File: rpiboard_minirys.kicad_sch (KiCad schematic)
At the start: 42 parts, among them IC1 LM51231QRGRRQ1, J1 Conn_01x01_Pin, J2 Conn_01x01_Pin, J3 Conn_01x01_Pin, J4 Conn_01x01_Pin, J6 MCU_Connector, Q1 ISK057N04LM6ATLA1, Q2 ISK057N04LM6ATLA1

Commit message: Added required connectors for this version
Also did some file name changes
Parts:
- removed J1, J2, J3, J4: Conn_01x01_Pin, TestPoint:TestPoint_Pad_2.0x2.0mm, symbol Connector:Conn_01x01_Pin
- removed J6: MCU_Connector, Connector_PinSocket_2.54mm:PinSocket_1x04_P2.54mm_Vertical, symbol Connector:Conn_01x04_Pin
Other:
- sheet 5V_Logic_Power renamed Supply_5V
- sheet Capacitor_Banks renamed Supply_24V_Capacitor_Banks
- sheet RPi_Connectors renamed Connectors
- sheet Connectors: file rpi_connectors.kicad_sch -> connectors.kicad_sch
- sheet Connectors ports: added +5V; removed none
- sheet Supply_24V_Capacitor_Banks: file capacitor_banks.kicad_sch -> s24v_capacitor_banks.kicad_sch
- sheet Supply_5V: file 5v_logic_power.kicad_sch -> supply_5v.kicad_sch
- sheet Supply_5V ports: added +5V; removed none
- note removed: "MCU Connector"
- title: Power Supply Module with 24V+5V output -> 24V Supply
- moved on the sheet: C5, C6, C8, R10, R11, R12, R3, R4, R5, R8, R9, TP4

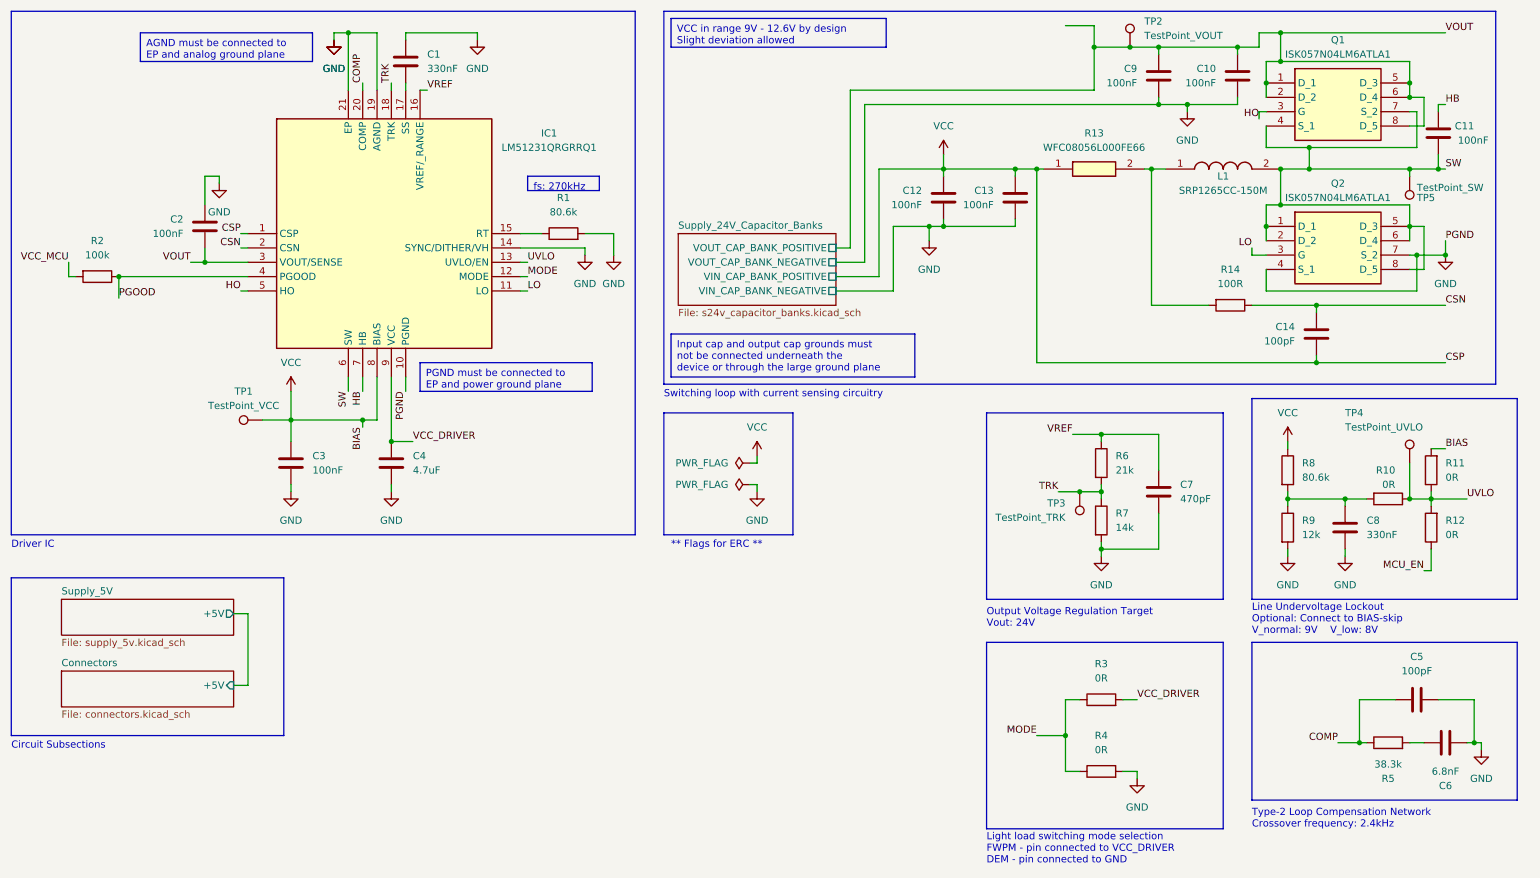
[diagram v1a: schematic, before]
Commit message: Finished motor drivers schematic
Still need to connect all the connectors and sort out old unused connections
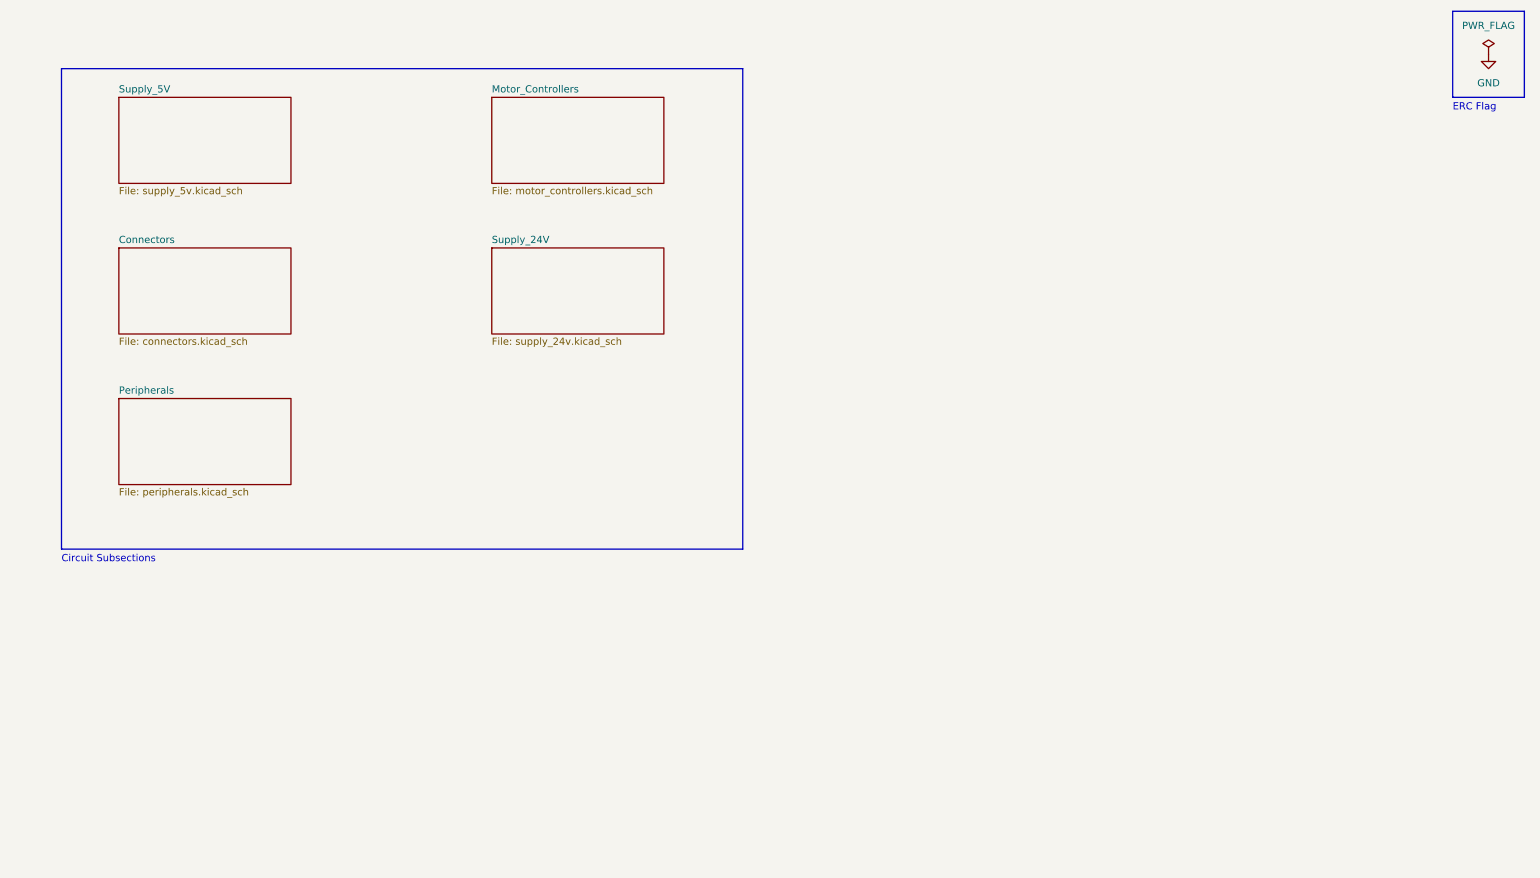
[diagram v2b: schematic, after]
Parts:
- removed C1, C8: 330nF, Capacitor_SMD:C_0603_1608Metric, symbol Device:C
- removed C10, C11, C12, C13, C2, C3, C9: 100nF, Capacitor_SMD:C_0603_1608Metric, symbol Device:C
- removed C14, C5: 100pF, Capacitor_SMD:C_0603_1608Metric, symbol Device:C
- removed C4: 4.7uF, Capacitor_SMD:C_0805_2012Metric, symbol Device:C
- removed C6: 6.8nF, Capacitor_SMD:C_0603_1608Metric, symbol Device:C
- removed C7: 470pF, Capacitor_SMD:C_0603_1608Metric, symbol Device:C
- removed IC1: LM51231QRGRRQ1, parts:QFN50P350X350X100-21N-D, symbol parts:LM51231QRGRRQ1
- removed L1: SRP1265CC-150M, parts:INDPM135125X650N, symbol parts:SRP1265CC-150M
- removed Q1: ISK057N04LM6ATLA1, parts:ISK057N04LM6ATLA1, symbol parts:ISK057N04LM6ATLA1
- removed Q2: ISK057N04LM6ATLA1, parts:ISK057N04LM6ATLA1, symbol SamacSys_Parts:ISK057N04LM6ATLA1
- removed R1, R8: 80.6k, Resistor_SMD:R_0603_1608Metric, symbol Device:R
- removed R10, R11, R12, R3, R4: 0R, Resistor_SMD:R_0603_1608Metric, symbol Device:R
- removed R13: WFC08056L000FE66, parts:RESC2013X85N, symbol parts:WFC08056L000FE66
- removed R14: 100R, Resistor_SMD:R_0603_1608Metric, symbol Device:R
- removed R2: 100k, Resistor_SMD:R_0603_1608Metric, symbol Device:R
- removed R5: 38.3k, Resistor_SMD:R_0603_1608Metric, symbol Device:R
- removed R6: 21k, Resistor_SMD:R_0603_1608Metric, symbol Device:R
- removed R7: 14k, Resistor_SMD:R_0603_1608Metric, symbol Device:R
- removed R9: 12k, Resistor_SMD:R_0603_1608Metric, symbol Device:R
- removed TP1: TestPoint_VCC, TestPoint:TestPoint_Pad_D1.0mm, symbol Connector:TestPoint
- removed TP2: TestPoint_VOUT, TestPoint:TestPoint_Pad_D1.0mm, symbol Connector:TestPoint
- removed TP3: TestPoint_TRK, TestPoint:TestPoint_Pad_D1.0mm, symbol Connector:TestPoint
- removed TP4: TestPoint_UVLO, TestPoint:TestPoint_Pad_D1.0mm, symbol Connector:TestPoint
- removed TP5: TestPoint_SW, TestPoint:TestPoint_Pad_D1.0mm, symbol Connector:TestPoint
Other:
- removed sheet Supply_24V_Capacitor_Banks
- added sheet Motor_Controllers (motor_controllers.kicad_sch)
- added sheet Peripherals (peripherals.kicad_sch)
- added sheet Supply_24V (supply_24v.kicad_sch)
- sheet Connectors ports: added none; removed +5V
- sheet Supply_5V ports: added none; removed +5V
- note added: "ERC Flag"
- note removed: "** Flags for ERC **"
- note removed: "Driver IC"
- note removed: "Light load switching mode selection FWPM - pin connected to VCC_DRIVER DEM - pin connected to GND"
- note removed: "Line Undervoltage Lockout Optional: Connect to BIAS-skip V_normal: 9V V_low: 8V"
- note removed: "Output Voltage Regulation Target Vout: 24V"
- note removed: "Switching loop with current sensing circuitry"
- note removed: "Type-2 Loop Compensation Network Crossover frequency: 2.4kHz"
- title: 24V Supply -> RPi Hat for MiniRys

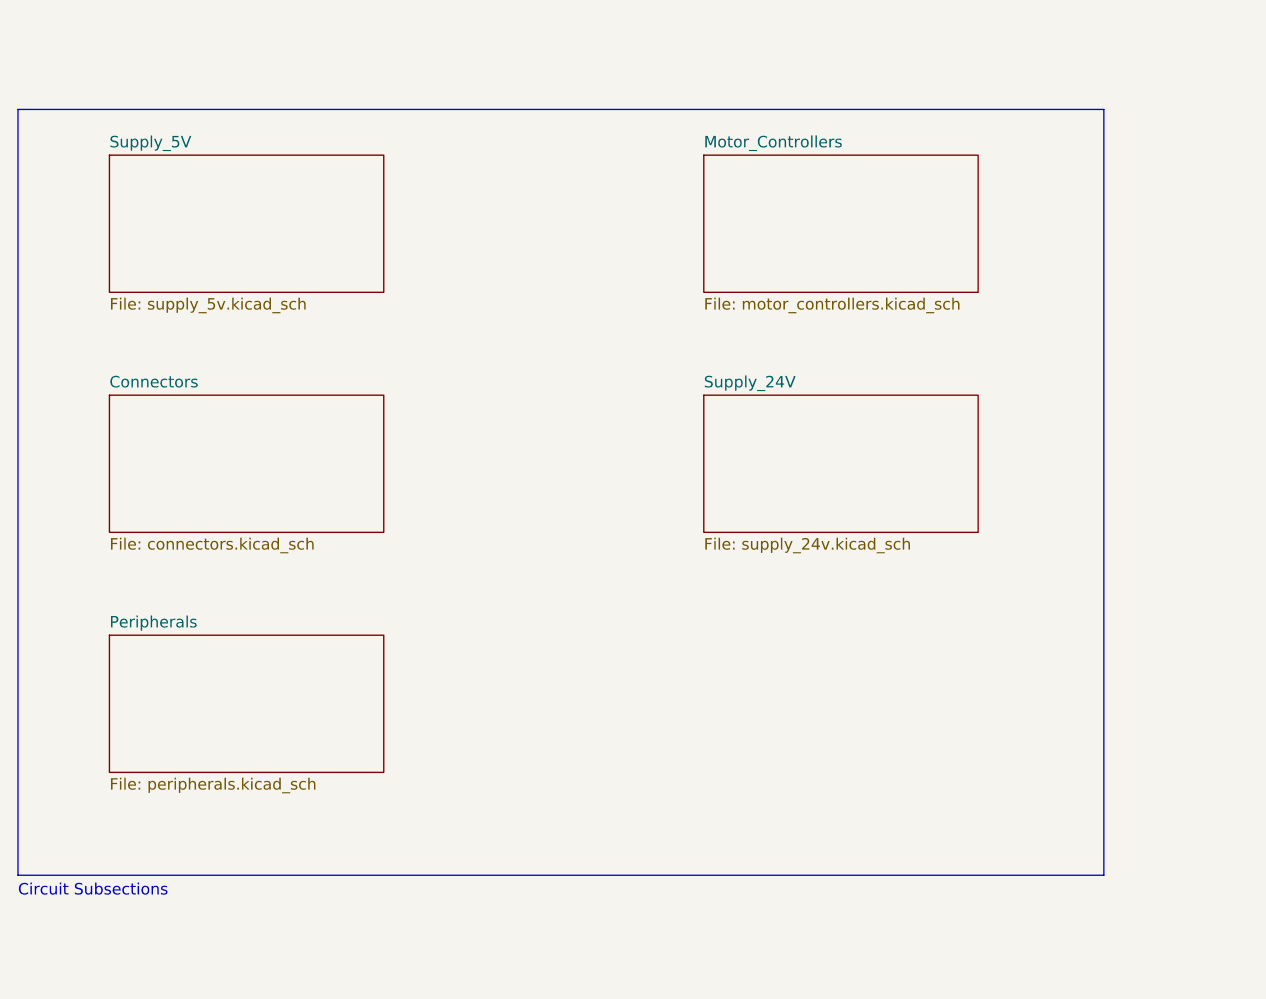
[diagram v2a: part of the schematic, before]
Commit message: New complete schematic version
May need to resize the resistors, also need to change the caps back to electrolytic
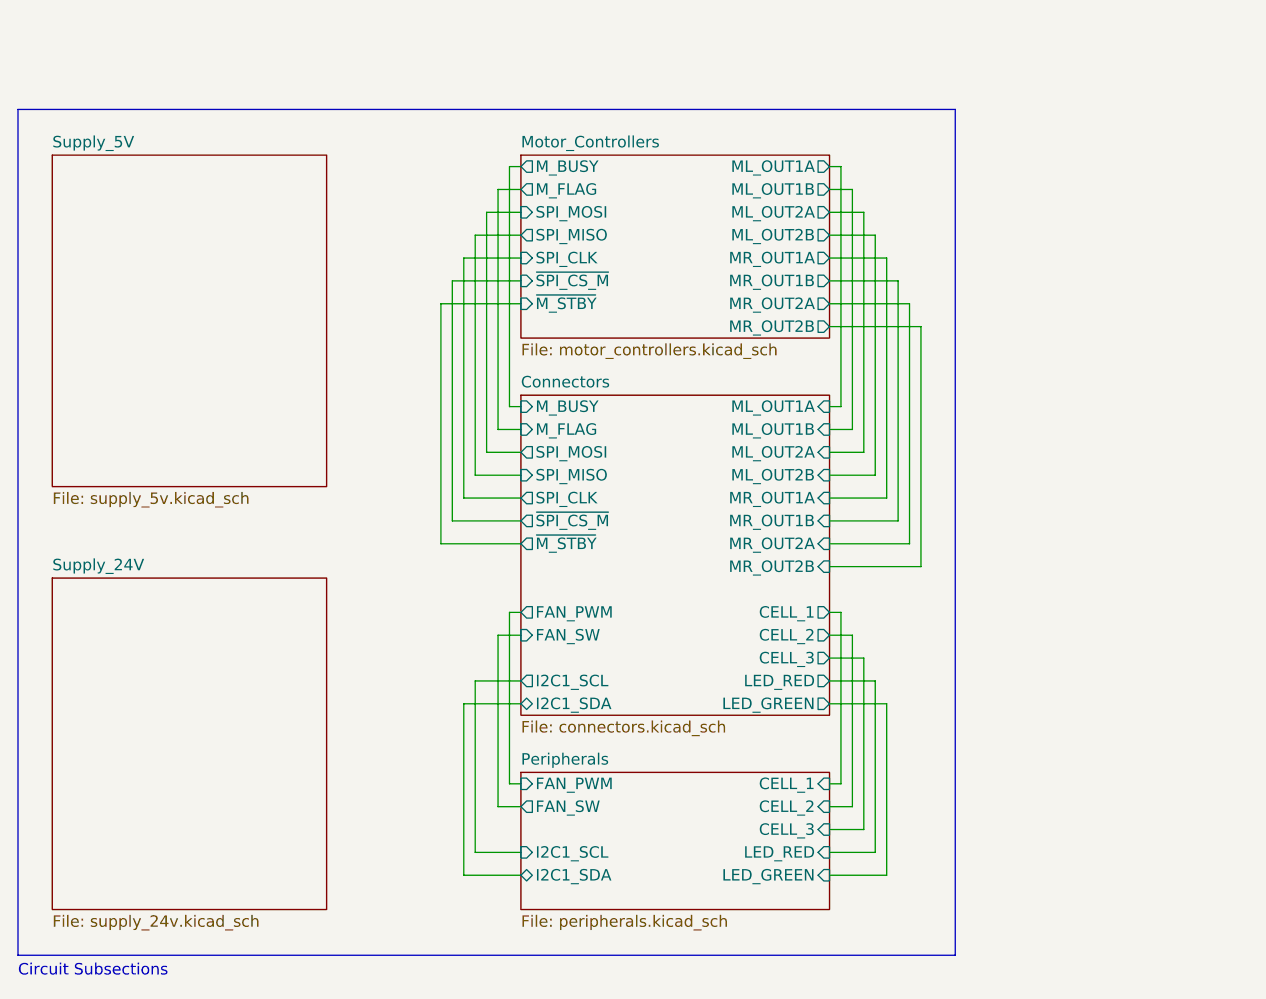
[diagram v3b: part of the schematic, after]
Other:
- sheet Connectors ports: added CELL_1, CELL_2, CELL_3, FAN_PWM, FAN_SW, I2C1_SCL, I2C1_SDA, LED_GREEN, LED_RED, ML_OUT1A, ML_OUT1B, ML_OUT2A, ML_OUT2B, MR_OUT1A, MR_OUT1B, MR_OUT2A, MR_OUT2B, M_BUSY, M_FLAG, SPI_CLK, SPI_MISO, SPI_MOSI, ~{M_STBY}, ~{SPI_CS_M}; removed none
- sheet Motor_Controllers ports: added ML_OUT1A, ML_OUT1B, ML_OUT2A, ML_OUT2B, MR_OUT1A, MR_OUT1B, MR_OUT2A, MR_OUT2B, M_BUSY, M_FLAG, SPI_CLK, SPI_MISO, SPI_MOSI, ~{M_STBY}, ~{SPI_CS_M}; removed none
- sheet Peripherals ports: added CELL_1, CELL_2, CELL_3, FAN_PWM, FAN_SW, I2C1_SCL, I2C1_SDA, LED_GREEN, LED_RED; removed none

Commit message: Uploaded all project files, finished PCB design
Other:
- note added: "GND ERC Flag"
- note removed: "ERC Flag"
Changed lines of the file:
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@@
   (title_block
     (title "RPi Hat for MiniRys")
-    (date "2023-11-29")
-    (rev "6.0")
+    (date "2024-01-27")
+    (rev "xx")
     (company "Kamil Adam Jabłoński")
   )
@@
     (fill (type none))
   )
-  (rectangle (start 270.51 13.97) (end 283.21 29.21)
+  (rectangle (start 267.97 13.97) (end 283.21 29.21)
     (stroke (width 0) (type default))
     (fill (type none))
@@
     (effects (font (size 1.27 1.27)) (justify left bottom))
   )
-  (text "ERC Flag" (at 270.51 31.75 0)
+  (text "GND ERC Flag" (at 267.97 31.75 0)
     (effects (font (size 1.27 1.27)) (justify left bottom))
   )
-  (symbol (lib_id "power:GND") (at 276.86 21.59 0) (unit 1)
+  (symbol (lib_id "power:GND") (at 275.59 21.59 0) (unit 1)
     (in_bom yes) (on_board yes) (dnp no) (fields_autoplaced)
-    (property "Reference" "#PWR019" (at 276.86 27.94 0)
-      (effects (font (size 1.27 1.27)) hide)
-    )
-    (property "Value" "GND" (at 276.86 26.67 0)
+    (property "Reference" "#PWR019" (at 275.59 27.94 0)
+      (effects (font (size 1.27 1.27)) hide)
+    )
+    (property "Value" "GND" (at 275.59 26.67 0)
       (effects (font (size 1.27 1.27)))
     )
-    (property "Footprint" "" (at 276.86 21.59 0)
-      (effects (font (size 1.27 1.27)) hide)
-    )
-    (property "Datasheet" "" (at 276.86 21.59 0)
+    (property "Footprint" "" (at 275.59 21.59 0)
+      (effects (font (size 1.27 1.27)) hide)
+    )
+    (property "Datasheet" "" (at 275.59 21.59 0)
       (effects (font (size 1.27 1.27)) hide)
     )
@@
     )
   )
-  (symbol (lib_id "power:PWR_FLAG") (at 276.86 21.59 0) (unit 1)
+  (symbol (lib_id "power:PWR_FLAG") (at 275.59 21.59 0) (unit 1)
     (in_bom yes) (on_board yes) (dnp no) (fields_autoplaced)
-    (property "Reference" "#FLG01" (at 276.86 19.685 0)
-      (effects (font (size 1.27 1.27)) hide)
-    )
-    (property "Value" "PWR_FLAG" (at 276.86 16.51 0)
+    (property "Reference" "#FLG01" (at 275.59 19.685 0)
+      (effects (font (size 1.27 1.27)) hide)
+    )
+    (property "Value" "PWR_FLAG" (at 275.59 16.51 0)
       (effects (font (size 1.27 1.27)))
     )
-    (property "Footprint" "" (at 276.86 21.59 0)
-      (effects (font (size 1.27 1.27)) hide)
-    )
-    (property "Datasheet" "~" (at 276.86 21.59 0)
-      (effects (font (size 1.27 1.27)) hide)
-    )
+    (property "Footprint" "" (at 275.59 21.59 0)
+      (effects (font (size 1.27 1.27)) hide)
+    )
+    (property "Datasheet" "~" (at 275.59 21.59 0)
+      (effects (font (size 1.27 1.27)) hide)
+    )
